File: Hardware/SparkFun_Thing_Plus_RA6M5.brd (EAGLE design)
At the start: 22.9 x 68.6 mm, 183 parts, among them J1 USB Female Type C Connector, J2 THING_PLUS_LOGICAL, J3 QWIIC_RA, J4 CONN_03X2, J7 MICRO-SDFRICTION, Q1 20V/4.2A/52mΩ/1.4W, Q2 20V/4.2A/52mΩ/1.4W, U1 R7FA6M5, U2 DA14531MOD, U3 MCP73831, U4 RT9080-33GJ5, U5 W25QXX128MBIT-6X5, U6 RT9080-33GJ5, U7 MAX17048, U8 LM66200, Y1 24.000MHz, Y2 32.768kHz

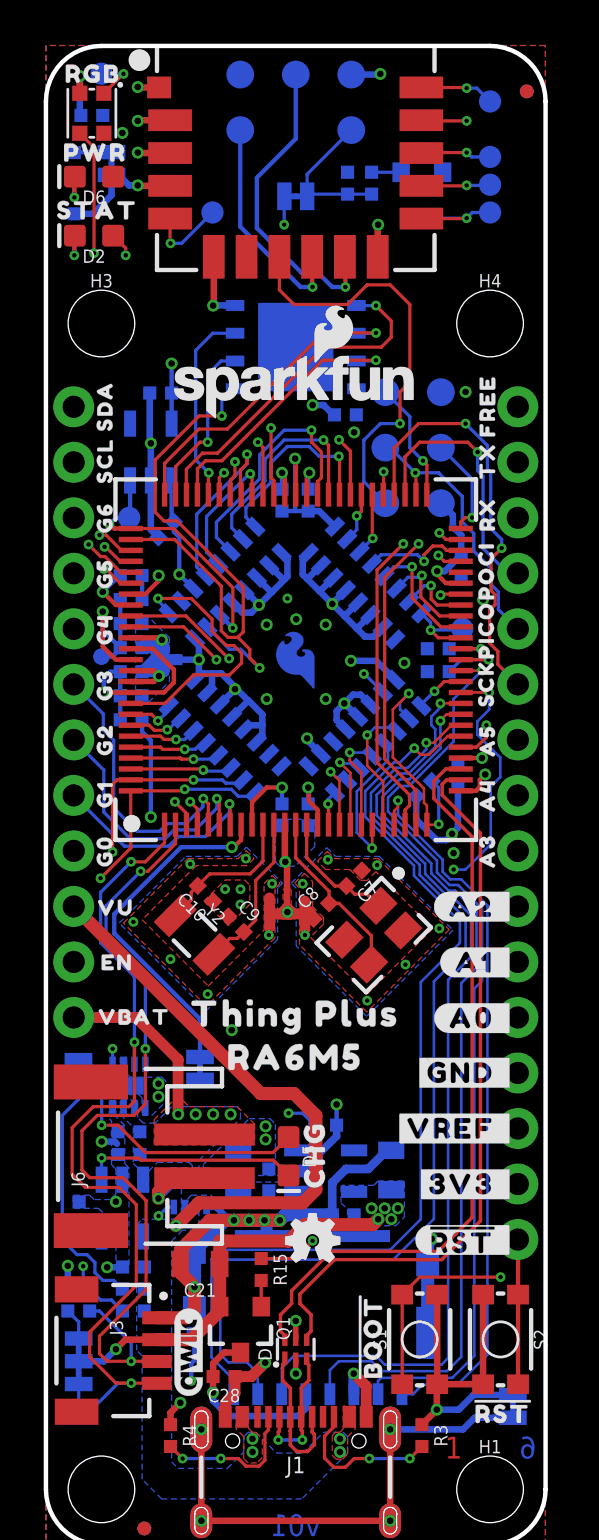
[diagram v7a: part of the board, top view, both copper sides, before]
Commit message: Post design review, pre-design review changes.
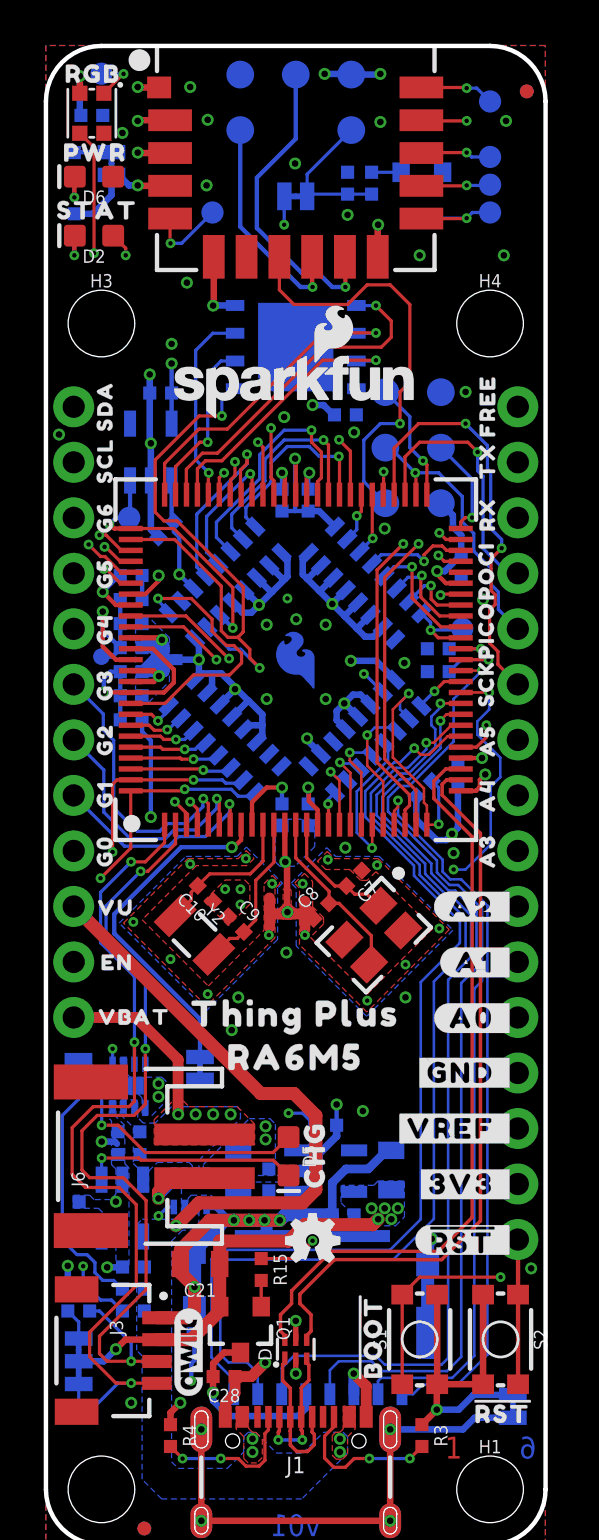
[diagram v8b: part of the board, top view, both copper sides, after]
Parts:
- added U$82: (no value), output:RA6M50
- added U$83: (no value), output:THING0
- added U$84: (no value), output:PLUS0
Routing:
- net GND: track 155.8 -> 157.9 mm, vias 44 -> 50
- net 3.3V: vias 20 -> 37
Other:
- board text added: "Layers: 6 Stackup: JLC06161H-3313 Material: TG155 Outer Layers: 1oz Inner Layers: 0.5oz Board thickness: 1.6mm Via Covering: Epoxy Filled & Capped Soldermask: Red Silkscreen: White Surface Finish: ENIG"
- board text removed: "Layers: 6 Stackup: JLC06161H-3313 Material: TG155 Outer Layers: 1oz Innter Layers: 0.5oz Board thickness: 1.6mm Via Covering: Epoxy Filled & Capped Soldermask: Red Silkscreen: White Surface Finish: ENIG"
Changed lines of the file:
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@@
 Material: TG155
 Outer Layers: 1oz
-Innter Layers: 0.5oz
+Inner Layers: 0.5oz
 Board thickness: 1.6mm
 Via Covering: Epoxy Filled &amp; Capped
@@
 <element name="U$9" library="output" package="SWD_RA6M50" value="" x="16.8" y="50.25" smashed="yes" rot="MR90"/>
 <element name="U$10" library="output" package="SWD_BLE0" value="" x="11.4" y="65.95" smashed="yes" rot="MR0"/>
+<element name="U$82" library="output" package="RA6M50" value="" x="11.43" y="28.5" smashed="yes" rot="MR0"/>
+<element name="U$83" library="output" package="THING0" value="" x="14.4" y="31.25" smashed="yes" rot="MR0"/>
+<element name="U$84" library="output" package="PLUS0" value="" x="8.35" y="31.25" smashed="yes" rot="MR0"/>
 </elements>
 <signals>
@@
 <wire x1="12.03" y1="34.62" x2="12" y2="34.65" width="0.2" layer="1"/>
 <wire x1="12.03" y1="34.03170625" x2="12.03" y2="34.62" width="0.2" layer="1"/>
+<via x="11" y="27.1" extent="1-16" drill="0.3"/>
+<via x="16.45" y="25.05" extent="1-16" drill="0.3"/>
+<via x="8.8" y="25.05" extent="1-16" drill="0.3"/>
+<via x="14.5" y="19.85" extent="1-16" drill="0.3"/>
+<via x="13.7" y="31.9" extent="1-16" drill="0.3"/>
+<via x="10.9" y="51.6" extent="1-16" drill="0.3"/>
+<via x="5.75" y="54.95" extent="1-16" drill="0.3"/>
+<via x="7.4" y="65.2" extent="1-16" drill="0.3"/>
+<via x="6.6" y="66.7" extent="1-16" drill="0.3"/>
+<via x="7.35" y="62.2" extent="1-16" drill="0.3"/>
+<via x="15.3" y="65.1" extent="1-16" drill="0.3"/>
+<via x="11.4" y="63.2" extent="1-16" drill="0.3"/>
+<via x="13.8" y="60.85" extent="1-16" drill="0.3"/>
+<via x="17.1" y="59" extent="1-16" drill="0.3"/>
+<via x="20.95" y="59" extent="1-16" drill="0.3"/>
+<via x="21.05" y="65.15" extent="1-16" drill="0.3"/>
+<via x="6.45" y="57.75" extent="1-16" drill="0.3"/>
 </signal>
 <signal name="!RA6M5_RESET!">
@@
 <wire x1="17.00335" y1="43.45335" x2="18.05335" y2="43.45335" width="0.15" layer="14"/>
 <wire x1="17.00335" y1="43.45335" x2="15.72835" y2="44.72835" width="0.15" layer="14"/>
-<wire x1="15.72835" y1="46.02835" x2="15.72835" y2="44.72835" width="0.15" layer="14"/>
+<wire x1="15.72835" y1="45.92835" x2="15.72835" y2="44.72835" width="0.15" layer="14"/>
 <wire x1="20.39" y1="50.87" x2="20.39" y2="49.34" width="0.15" layer="14"/>
 <wire x1="20.39" y1="49.34" x2="19.35" y2="48.3" width="0.15" layer="14"/>
-<wire x1="19.35" y1="48.3" x2="18" y2="48.3" width="0.15" layer="14"/>
-<wire x1="18" y1="48.3" x2="15.72835" y2="46.02835" width="0.15" layer="14"/>
+<wire x1="19.35" y1="48.3" x2="18.1" y2="48.3" width="0.15" layer="14"/>
+<wire x1="18.1" y1="48.3" x2="15.72835" y2="45.92835" width="0.15" layer="14"/>
 </signal>
 <signal name="GND" class="4">
@@
 <wire x1="11.03" y1="31.17" x2="10.95" y2="31.25" width="0.3" layer="1"/>
 <wire x1="11.03" y1="29.37" x2="11.03" y2="31.17" width="0.3" layer="1"/>
-<wire x1="10.93" y1="32.95" x2="10.93" y2="31.27" width="0.3" layer="1"/>
+<wire x1="10.93" y1="32.95" x2="10.93" y2="31.27" width="0.25" layer="1"/>
 <wire x1="10.95" y1="31.25" x2="10.93" y2="31.27" width="0.3" layer="1"/>
 <contactref element="RN4" pad="8"/>
@@
 <wire x1="4.8" y1="50.4" x2="4.75" y2="50.45" width="0.3" layer="16"/>
 <wire x1="4.75" y1="50.45" x2="4.75" y2="52.7" width="0.3" layer="16"/>
+<via x="3.9" y="6.5" extent="1-16" drill="0.3"/>
+<via x="22.2" y="12.65" extent="1-16" drill="0.3"/>
+<via x="15.5" y="46.5" extent="1-16" drill="0.3"/>
+<via x="4.75" y="53.55" extent="1-16" drill="0.3"/>
+<wire x1="4.75" y1="52.7" x2="4.75" y2="53.55" width="0.3" layer="16"/>
+<via x="0.6" y="50.8" extent="1-16" drill="0.3"/>
+<via x="12.75" y="67.3" extent="1-16" drill="0.3"/>
+<wire x1="12.75" y1="67.3" x2="13.94" y2="67.3" width="0.3" layer="16"/>
+<wire x1="13.94" y1="67.3" x2="13.97" y2="67.27" width="0.2" layer="16"/>
 </signal>
 <signal name="N$1">
